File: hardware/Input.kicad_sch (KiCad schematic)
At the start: 15 parts, among them J10 Conn_Coaxial, J11 Conn_Coaxial, J12 Conn_Coaxial, J13 Conn_Coaxial, U22 SN74LVC2T45DCTR, U23 SN74LVC2T45DCTR

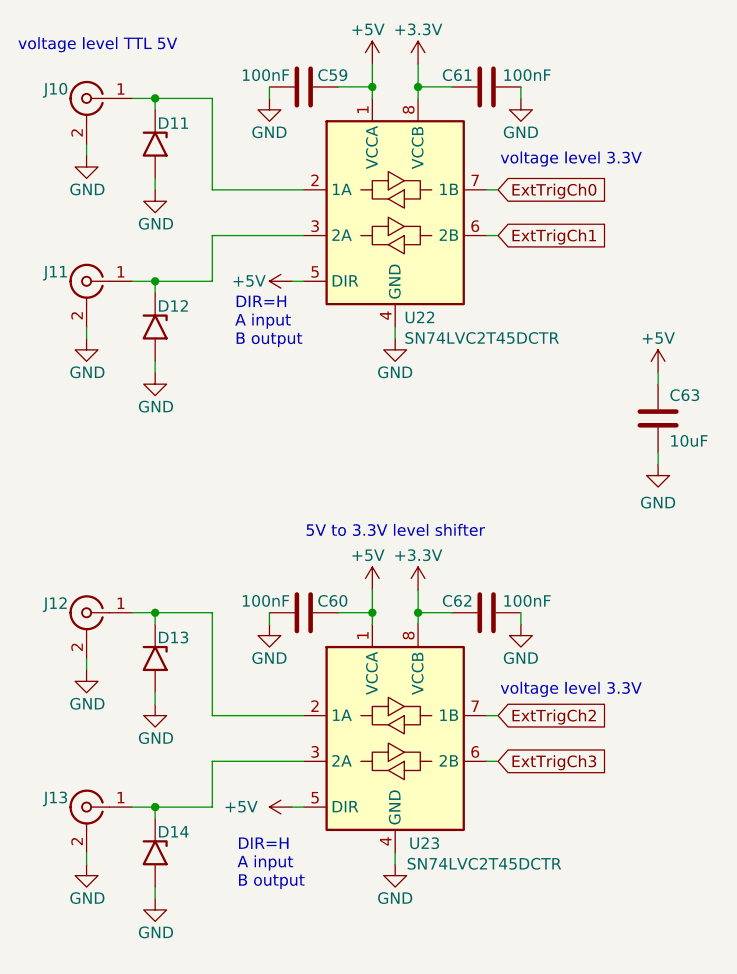
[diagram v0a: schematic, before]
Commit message: add pulldowns to external triggers
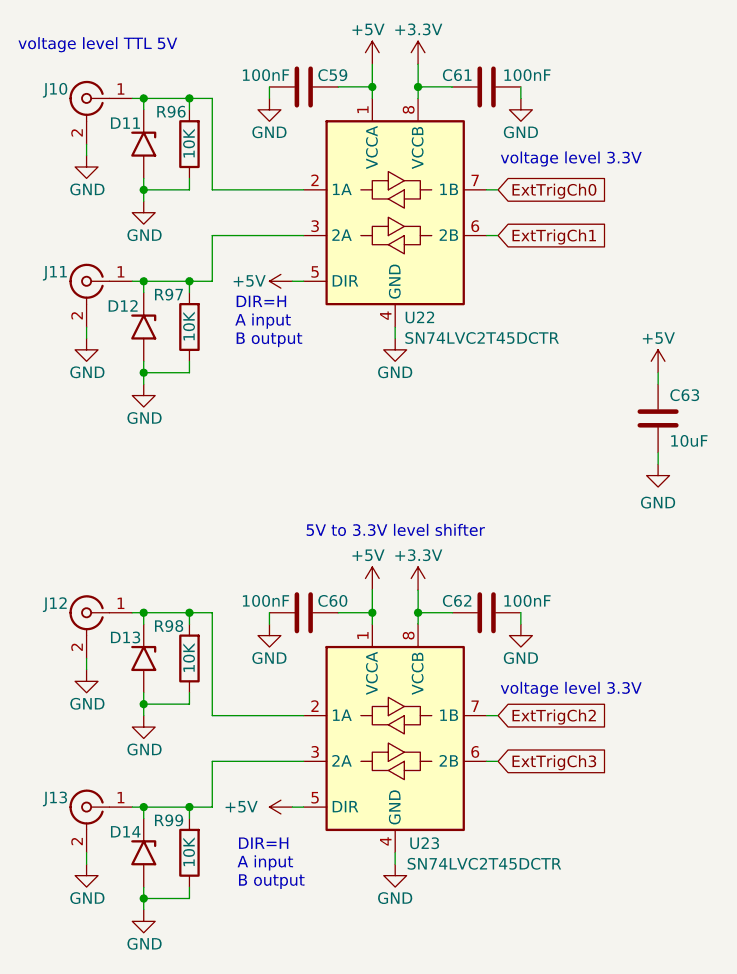
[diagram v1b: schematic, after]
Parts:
- added R96, R97, R98, R99: 10K, Resistor_SMD:R_0402_1005Metric, symbol Device:R
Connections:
- net GND: now also R96.1, R97.1, R98.1, R99.1
- net at D14.1 (A1), J13.1 (In), U23.3 (2A): now also R99.2
- net at D11.1 (A1), J10.1 (In), U22.2 (1A): now also R96.2
- net at D12.1 (A1), J11.1 (In), U22.3 (2A): now also R97.2
- net at D13.1 (A1), J12.1 (In), U23.2 (1A): now also R98.2
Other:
- moved on the sheet: D11, D12, D13, D14

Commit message: update 1K, 31K6, 10K resistors to 0.1%
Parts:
- R96, R97, R98, R99: Link https://www.digikey.com/en/products/detail/samsung-electro-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 -> https://www.digikey.com/en/products/detail/yageo/RT0402BRD0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; Manufacturer Samsung Electro-Mechanics -> YAGEO; Manufacturer Number RC1005F103CS -> RT0402BRD0710KL; Tolerance (none) -> 0.1%
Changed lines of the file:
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@@
 			)
 		)
-		(property "Datasheet" "https://mm.digikey.com/Volume0/opasdata/d220001/medias/docus/39/RC_Series_ds.pdf"
+		(property "Datasheet" "https://yageogroup.com/content/datasheet/asset/file/PYU-RT_1-TO-0-01_ROHS_L"
 			(at 129.54 121.92 0)
 			(effects
@@
 			)
 		)
-		(property "Manufacturer" "Samsung Electro-Mechanics"
+		(property "Manufacturer" "YAGEO"
 			(at 129.54 121.92 0)
 			(effects
@@
 			)
 		)
-		(property "Manufacturer Number" "RC1005F103CS"
+		(property "Manufacturer Number" "RT0402BRD0710KL"
 			(at 129.54 121.92 0)
 			(effects
@@
 			)
 		)
-		(property "Link" "https://www.digikey.com/en/products/detail/samsung-electro-mechanics/RC1005F103CS/3903439"
+		(property "Link" "https://www.digikey.com/en/products/detail/yageo/RT0402BRD0710KL/1068998"
 			(at 129.54 121.92 0)
 			(effects
@@
 		)
 		(property "Supplier Link" ""
+			(at 129.54 121.92 0)
+			(effects
+				(font
+					(size 1.27 1.27)
+				)
+				(hide yes)
+			)
+		)
+		(property "Tolerance" "0.1%"
 			(at 129.54 121.92 0)
 			(effects
@@
 			)
 		)
-		(property "Datasheet" "https://mm.digikey.com/Volume0/opasdata/d220001/medias/docus/39/RC_Series_ds.pdf"
+		(property "Datasheet" "https://yageogroup.com/content/datasheet/asset/file/PYU-RT_1-TO-0-01_ROHS_L"
 			(at 129.54 143.51 0)
 			(effects
@@
 			)
 		)
-		(property "Manufacturer" "Samsung Electro-Mechanics"
+		(property "Manufacturer" "YAGEO"
 			(at 129.54 143.51 0)
 			(effects
@@
 			)
 		)
-		(property "Manufacturer Number" "RC1005F103CS"
+		(property "Manufacturer Number" "RT0402BRD0710KL"
 			(at 129.54 143.51 0)
 			(effects
@@
 			)
 		)
-		(property "Link" "https://www.digikey.com/en/products/detail/samsung-electro-mechanics/RC1005F103CS/3903439"
+		(property "Link" "https://www.digikey.com/en/products/detail/yageo/RT0402BRD0710KL/1068998"
 			(at 129.54 143.51 0)
 			(effects
@@
 		)
 		(property "Supplier Link" ""
+			(at 129.54 143.51 0)
+			(effects
+				(font
+					(size 1.27 1.27)
+				)
+				(hide yes)
+			)
+		)
+		(property "Tolerance" "0.1%"
 			(at 129.54 143.51 0)
 			(effects
@@
 			)
 		)
-		(property "Datasheet" "https://mm.digikey.com/Volume0/opasdata/d220001/medias/docus/39/RC_Series_ds.pdf"
+		(property "Datasheet" "https://yageogroup.com/content/datasheet/asset/file/PYU-RT_1-TO-0-01_ROHS_L"
 			(at 129.54 85.09 0)
 			(effects
@@
 			)
 		)
-		(property "Manufacturer" "Samsung Electro-Mechanics"
+		(property "Manufacturer" "YAGEO"
 			(at 129.54 85.09 0)
 			(effects
@@
 			)
 		)
-		(property "Manufacturer Number" "RC1005F103CS"
+		(property "Manufacturer Number" "RT0402BRD0710KL"
 			(at 129.54 85.09 0)
 			(effects
@@
 			)
 		)
-		(property "Link" "https://www.digikey.com/en/products/detail/samsung-electro-mechanics/RC1005F103CS/3903439"
+		(property "Link" "https://www.digikey.com/en/products/detail/yageo/RT0402BRD0710KL/1068998"
 			(at 129.54 85.09 0)
 			(effects
@@
 		)
 		(property "Supplier Link" ""
+			(at 129.54 85.09 0)
+			(effects
+				(font
+					(size 1.27 1.27)
+				)
+				(hide yes)
+			)
+		)
+		(property "Tolerance" "0.1%"
 			(at 129.54 85.09 0)
 			(effects
@@
 			)
 		)
-		(property "Datasheet" "https://mm.digikey.com/Volume0/opasdata/d220001/medias/docus/39/RC_Series_ds.pdf"
+		(property "Datasheet" "https://yageogroup.com/content/datasheet/asset/file/PYU-RT_1-TO-0-01_ROHS_L"
 			(at 129.54 64.77 0)
 			(effects
@@
 			)
 		)
-		(property "Manufacturer" "Samsung Electro-Mechanics"
+		(property "Manufacturer" "YAGEO"
 			(at 129.54 64.77 0)
 			(effects
@@
 			)
 		)
-		(property "Manufacturer Number" "RC1005F103CS"
+		(property "Manufacturer Number" "RT0402BRD0710KL"
 			(at 129.54 64.77 0)
 			(effects
@@
 			)
 		)
-		(property "Link" "https://www.digikey.com/en/products/detail/samsung-electro-mechanics/RC1005F103CS/3903439"
+		(property "Link" "https://www.digikey.com/en/products/detail/yageo/RT0402BRD0710KL/1068998"
 			(at 129.54 64.77 0)
 			(effects
@@
 			(at 129.54 64.77 0)
 			(effects
+				(font
+					(size 1.27 1.27)
+				)
+				(hide yes)
+			)
+		)
+		(property "Tolerance" "0.1%"
+			(at 129.54 64.77 0)
+			(effects

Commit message: swap BNC connectors to taller versions
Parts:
- J10, J11, J12, J13: footprint kicad-lib:BNC_TEConnectivity_CONBNC001_Vertical -> kicad-lib:BNC_AmphenolRF_031-5329-52RFX_Vertical; Link https://www.digikey.com/en/products/detail/te-connectivity-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 -> https://www.digikey.com/en/products/detail/amphenol-rf/031-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; Manufacturer TE Connectivity Linx -> Amphenol RF
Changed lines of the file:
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@@
 			)
 		)
-		(property "Footprint" "kicad-lib:BNC_TEConnectivity_CONBNC001_Vertical"
+		(property "Footprint" "kicad-lib:BNC_AmphenolRF_031-5329-52RFX_Vertical"
 			(at 118.11 138.43 0)
 			(effects
@@
 			)
 		)
-		(property "Datasheet" "https://www.te.com/commerce/DocumentDelivery/DDEController?Action=srchrtrv&DocNm=CONBNC001&DocType=Data+Sheet&DocLang=English&DocFormat=pdf&PartCntxt=CONBNC001"
+		(property "Datasheet" "https://www.amphenolrf.com/en-us/assets/file/4065788070/"
 			(at 118.11 138.43 0)
 			(effects
@@
 			)
 		)
-		(property "Link" "https://www.digikey.com/en/products/detail/te-connectivity-linx/CONBNC001/16013844"
+		(property "Link" "https://www.digikey.com/en/products/detail/amphenol-rf/031-5329-52RFX/2041814"
 			(at 118.11 138.43 0)
 			(effects
@@
 			)
 		)
-		(property "Manufacturer" "TE Connectivity Linx"
+		(property "Manufacturer" "Amphenol RF"
 			(at 118.11 138.43 0)
 			(effects
@@
 			)
 		)
-		(property "Footprint" "kicad-lib:BNC_TEConnectivity_CONBNC001_Vertical"
+		(property "Footprint" "kicad-lib:BNC_AmphenolRF_031-5329-52RFX_Vertical"
 			(at 118.11 80.01 0)
 			(effects
@@
 			)
 		)
-		(property "Datasheet" "https://www.te.com/commerce/DocumentDelivery/DDEController?Action=srchrtrv&DocNm=CONBNC001&DocType=Data+Sheet&DocLang=English&DocFormat=pdf&PartCntxt=CONBNC001"
+		(property "Datasheet" "https://www.amphenolrf.com/en-us/assets/file/4065788070/"
 			(at 118.11 80.01 0)
 			(effects
@@
 			)
 		)
-		(property "Link" "https://www.digikey.com/en/products/detail/te-connectivity-linx/CONBNC001/16013844"
+		(property "Link" "https://www.digikey.com/en/products/detail/amphenol-rf/031-5329-52RFX/2041814"
 			(at 118.11 80.01 0)
 			(effects
@@
 			)
 		)
-		(property "Manufacturer" "TE Connectivity Linx"
+		(property "Manufacturer" "Amphenol RF"
 			(at 118.11 80.01 0)
 			(effects
@@
 			)
 		)
-		(property "Footprint" "kicad-lib:BNC_TEConnectivity_CONBNC001_Vertical"
+		(property "Footprint" "kicad-lib:BNC_AmphenolRF_031-5329-52RFX_Vertical"
 			(at 118.11 116.84 0)
 			(effects
@@
 			)
 		)
-		(property "Datasheet" "https://www.te.com/commerce/DocumentDelivery/DDEController?Action=srchrtrv&DocNm=CONBNC001&DocType=Data+Sheet&DocLang=English&DocFormat=pdf&PartCntxt=CONBNC001"
+		(property "Datasheet" "https://www.amphenolrf.com/en-us/assets/file/4065788070/"
 			(at 118.11 116.84 0)
 			(effects
@@
 			)
 		)
-		(property "Link" "https://www.digikey.com/en/products/detail/te-connectivity-linx/CONBNC001/16013844"
+		(property "Link" "https://www.digikey.com/en/products/detail/amphenol-rf/031-5329-52RFX/2041814"
 			(at 118.11 116.84 0)
 			(effects
@@
 			)
 		)
-		(property "Manufacturer" "TE Connectivity Linx"
+		(property "Manufacturer" "Amphenol RF"
 			(at 118.11 116.84 0)
 			(effects
@@
 			)
 		)
-		(property "Footprint" "kicad-lib:BNC_TEConnectivity_CONBNC001_Vertical"
+		(property "Footprint" "kicad-lib:BNC_AmphenolRF_031-5329-52RFX_Vertical"
 			(at 118.11 59.69 0)
 			(effects
@@
 			)
 		)
-		(property "Datasheet" "https://www.te.com/commerce/DocumentDelivery/DDEController?Action=srchrtrv&DocNm=CONBNC001&DocType=Data+Sheet&DocLang=English&DocFormat=pdf&PartCntxt=CONBNC001"
+		(property "Datasheet" "https://www.amphenolrf.com/en-us/assets/file/4065788070/"
 			(at 118.11 59.69 0)
 			(effects
@@
 			)
 		)
-		(property "Link" "https://www.digikey.com/en/products/detail/te-connectivity-linx/CONBNC001/16013844"
+		(property "Link" "https://www.digikey.com/en/products/detail/amphenol-rf/031-5329-52RFX/2041814"
 			(at 118.11 59.69 0)
 			(effects
@@
 			)
 		)
-		(property "Manufacturer" "TE Connectivity Linx"
+		(property "Manufacturer" "Amphenol RF"
 			(at 118.11 59.69 0)
 			(effects
